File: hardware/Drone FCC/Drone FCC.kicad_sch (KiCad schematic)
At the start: 4 parts

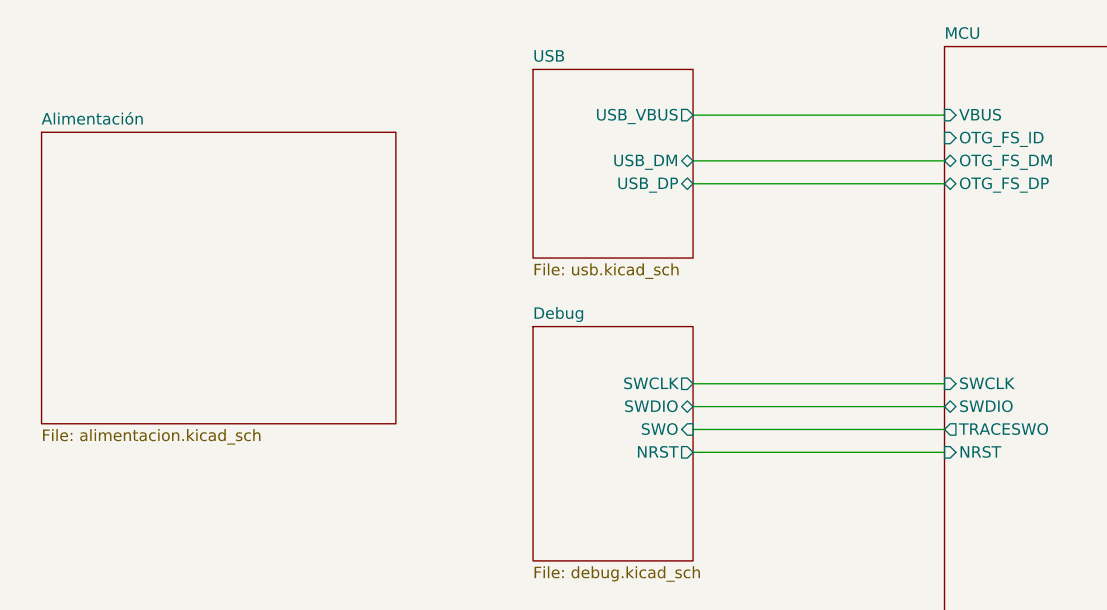
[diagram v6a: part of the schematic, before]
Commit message: add soft-start for USB connector
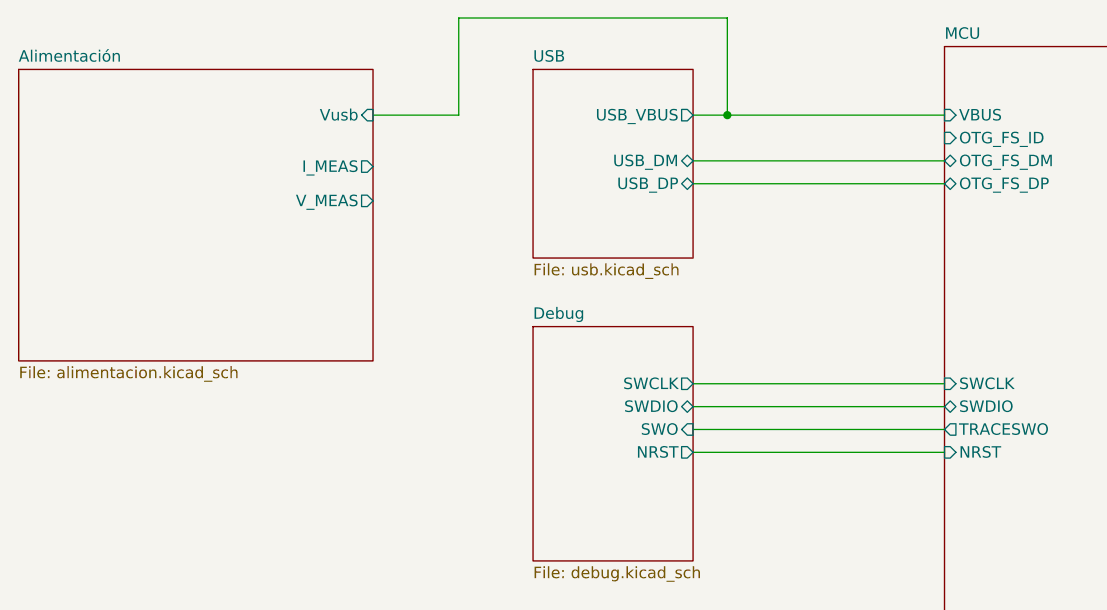
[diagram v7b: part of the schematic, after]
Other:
- sheet Alimentación ports: added I_MEAS, V_MEAS, Vusb; removed none
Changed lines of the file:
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@@
   (junction (at 194.31 17.145) (diameter 0) (color 0 0 0 0)
   )
+  (junction (at 94.615 24.765) (diameter 0) (color 0 0 0 0)
+  )
   (junction (at 185.42 17.145) (diameter 0) (color 0 0 0 0)
   )
@@
     (stroke (width 0) (type default) (color 0 0 0 0))
   )
+  (wire (pts (xy 64.77 13.97) (xy 94.615 13.97))
+    (stroke (width 0) (type default) (color 0 0 0 0))
+  )
   (wire (pts (xy 185.42 17.145) (xy 194.31 17.145))
     (stroke (width 0) (type default) (color 0 0 0 0))
   )
+  (wire (pts (xy 94.615 13.97) (xy 94.615 24.765))
+    (stroke (width 0) (type default) (color 0 0 0 0))
+  )
   (wire (pts (xy 194.31 17.145) (xy 203.2 17.145))
     (stroke (width 0) (type default) (color 0 0 0 0))
@@
     (stroke (width 0) (type default) (color 0 0 0 0))
   )
+  (wire (pts (xy 55.245 24.765) (xy 64.77 24.765))
+    (stroke (width 0) (type default) (color 0 0 0 0))
+  )
   (wire (pts (xy 90.17 127.635) (xy 101.6 127.635))
     (stroke (width 0) (type default) (color 0 0 0 0))
@@
     (stroke (width 0) (type default) (color 0 0 0 0))
   )
+  (wire (pts (xy 94.615 24.765) (xy 118.745 24.765))
+    (stroke (width 0) (type default) (color 0 0 0 0))
+  )
   (wire (pts (xy 176.53 34.925) (xy 217.805 34.925))
     (stroke (width 0) (type default) (color 0 0 0 0))
@@
     (stroke (width 0) (type default) (color 0 0 0 0))
   )
+  (wire (pts (xy 64.77 24.765) (xy 64.77 13.97))
+    (stroke (width 0) (type default) (color 0 0 0 0))
+  )
   (wire (pts (xy 203.2 17.145) (xy 206.375 17.145))
     (stroke (width 0) (type default) (color 0 0 0 0))
   )
-  (wire (pts (xy 90.805 24.765) (xy 118.745 24.765))
+  (wire (pts (xy 90.805 24.765) (xy 94.615 24.765))
     (stroke (width 0) (type default) (color 0 0 0 0))
   )
@@
     )
   )
-  (sheet (at 18.415 26.67) (size 39.37 32.385) (fields_autoplaced)
+  (sheet (at 15.875 19.685) (size 39.37 32.385) (fields_autoplaced)
     (stroke (width 0.1524) (type solid) (color 0 0 0 0))
     (fill (color 0 0 0 0.0000))
-    (property "Sheet name" "Alimentación" (id 0) (at 18.415 25.9584 0)
+    (property "Sheet name" "Alimentación" (id 0) (at 15.875 18.9734 0)
       (effects (font (size 1.27 1.27)) (justify left bottom))
     )
-    (property "Sheet file" "alimentacion.kicad_sch" (id 1) (at 18.415 59.6396 0)
+    (property "Sheet file" "alimentacion.kicad_sch" (id 1) (at 15.875 52.6546 0)
       (effects (font (size 1.27 1.27)) (justify left top))
+    )
+    (pin "Vusb" input (at 55.245 24.765 0)
+      (effects (font (size 1.27 1.27)) (justify right))
+    )
+    (pin "I_MEAS" output (at 55.245 30.48 0)
+      (effects (font (size 1.27 1.27)) (justify right))
+    )
+    (pin "V_MEAS" output (at 55.245 34.29 0)
+      (effects (font (size 1.27 1.27)) (justify right))
     )
   )
@@
       (reference "#PWR0126") (unit 1) (value "GND") (footprint "")
     )
+    (path "/72959738-982c-4565-97f6-d336a978e9e3/38bdc80e-0c02-4978-8b04-bb66b484b67a"
+      (reference "#PWR?") (unit 1) (value "GND") (footprint "")
+    )
+    (path "/72959738-982c-4565-97f6-d336a978e9e3/ea86a414-346a-49c6-bd7e-e9c2b4271744"
+      (reference "#PWR?") (unit 1) (value "GND") (footprint "")
+    )
     (path "/2dea4649-a03b-4105-a448-fdfd58cb624b/7430465c-9d48-4f87-807f-b7d872f0d403"
       (reference "C1") (unit 1) (value "0.1u") (footprint "")
@@
       (reference "C8") (unit 1) (value "1uF") (footprint "")
     )
+    (path "/72959738-982c-4565-97f6-d336a978e9e3/00ade61f-b970-4dc8-813c-a38cb45e0973"
+      (reference "C?") (unit 1) (value "0.1u") (footprint "")
+    )
+    (path "/72959738-982c-4565-97f6-d336a978e9e3/4f942f3b-aa43-4f4e-a46b-9d811ba7af71"
+      (reference "C?") (unit 1) (value "10u") (footprint "")
+    )
+    (path "/72959738-982c-4565-97f6-d336a978e9e3/5e07db7f-0418-40ce-8191-d91083077180"
+      (reference "C?") (unit 1) (value "1.6u") (footprint "")
+    )
+    (path "/72959738-982c-4565-97f6-d336a978e9e3/755a6007-876b-43d3-8115-b3483b43c004"
+      (reference "C?") (unit 1) (value "10p") (footprint "")
+    )
+    (path "/72959738-982c-4565-97f6-d336a978e9e3/baee0f21-030a-4cd1-9ab2-d5094fd98f6b"
+      (reference "C?") (unit 1) (value "100n") (footprint "")
+    )
+    (path "/72959738-982c-4565-97f6-d336a978e9e3/d7ca4ab6-80b6-4eea-bfc4-259718bc6183"
+      (reference "C?") (unit 1) (value "10u") (footprint "")
+    )
+    (path "/72959738-982c-4565-97f6-d336a978e9e3/e778241d-4070-4654-b25b-4ef8a2002459"
+      (reference "C?") (unit 1) (value "10p") (footprint "")
+    )
+    (path "/72959738-982c-4565-97f6-d336a978e9e3/0fea5a06-2f40-4fce-b388-8b4d86fb4553"
+      (reference "D?") (unit 1) (value "PMEG60T30ELRX ") (footprint "")
+    )
+    (path "/72959738-982c-4565-97f6-d336a978e9e3/88f1279e-9608-491a-afa4-f73a050ed3dd"
+      (reference "D?") (unit 1) (value "PMEG60T30ELRX ") (footprint "")
+    )
+    (path "/72959738-982c-4565-97f6-d336a978e9e3/f0f7f5f5-3f6e-48ca-b5e4-af3564804fdc"
+      (reference "D?") (unit 1) (value "PMEG60T30ELRX ") (footprint "")
+    )
     (path "/2dea4649-a03b-4105-a448-fdfd58cb624b/1ada52bf-3160-4b2e-8e93-ed65b64dff92"
       (reference "J1") (unit 1) (value "Mag Dupont") (footprint "Connector_PinHeader_2.54mm:PinHeader_2x03_P2.54mm_Horizontal")
@@
       (reference "J28") (unit 1) (value "PM02 PixHawk") (footprint "Connector_Hirose:Hirose_DF13C_CL535-0406-3-51_1x06-1MP_P1.25mm_Vertical")
     )
+    (path "/72959738-982c-4565-97f6-d336a978e9e3/0c0956d0-8805-4633-b8ad-65ce81b4ea74"
+      (reference "Q?") (unit 1) (value "Q_PMOS_GSD") (footprint "")
+    )
     (path "/9bc65728-e237-4f6c-82eb-0920dd4372d2"
       (reference "R1") (unit 1) (value "R") (footprint "")
@@
       (reference "R12") (unit 1) (value "82k") (footprint "")
     )
+    (path "/72959738-982c-4565-97f6-d336a978e9e3/2433dbd1-1e36-4567-b745-fd4f9a300193"
+      (reference "R?") (unit 1) (value "6.8k") (footprint "")
+    )
+    (path "/72959738-982c-4565-97f6-d336a978e9e3/32db09ad-b85d-43b0-b4d8-f440c84e9975"
+      (reference "R?") (unit 1) (value "10k") (footprint "")
+    )
+    (path "/72959738-982c-4565-97f6-d336a978e9e3/3cb4d06a-c4bd-4d7f-9da2-665afa7ce0e1"
+      (reference "R?") (unit 1) (value "1M") (footprint "")
+    )
+    (path "/72959738-982c-4565-97f6-d336a978e9e3/593dd5ec-837d-4755-a5b0-f86fb130da3d"
+      (reference "R?") (unit 1) (value "1M") (footprint "")
+    )
+    (path "/72959738-982c-4565-97f6-d336a978e9e3/5e60ef31-4892-4da8-9c6e-7d0d51e50fbd"
+      (reference "R?") (unit 1) (value "10") (footprint "")
+    )
+    (path "/72959738-982c-4565-97f6-d336a978e9e3/7d27e8d8-be6b-4576-8797-81702053f8d4"
+      (reference "R?") (unit 1) (value "33") (footprint "")
+    )
+    (path "/72959738-982c-4565-97f6-d336a978e9e3/c6e938f6-ee29-43b3-9164-7dc2aa66b146"
+      (reference "R?") (unit 1) (value "10k") (footprint "")
+    )
     (path "/2dea4649-a03b-4105-a448-fdfd58cb624b/526c1ffa-b5c3-4a19-b2e6-f432001e1abc"
